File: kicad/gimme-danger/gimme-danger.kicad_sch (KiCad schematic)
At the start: 4 parts, among them U1 ESP32-S3-WROOM-1, U2 TPD6S300RUKR, U3 U261-241N-4BS2SS

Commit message: Set up page details
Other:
- company: (none) -> rbaron.net
- title: (none) -> gimme-danger
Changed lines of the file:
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@@
 (kicad_sch (version 20230121) (generator eeschema)
   (paper "A4")
+  (title_block
+    (title "gimme-danger")
+    (date "2024-01-15")
+    (rev "0.0.1a")
+    (company "rbaron.net")
+  )
   (text "TODO\n- USB resistors (for termination + protection? 100 Ohm?)"
     (at 200.025 144.145 0)

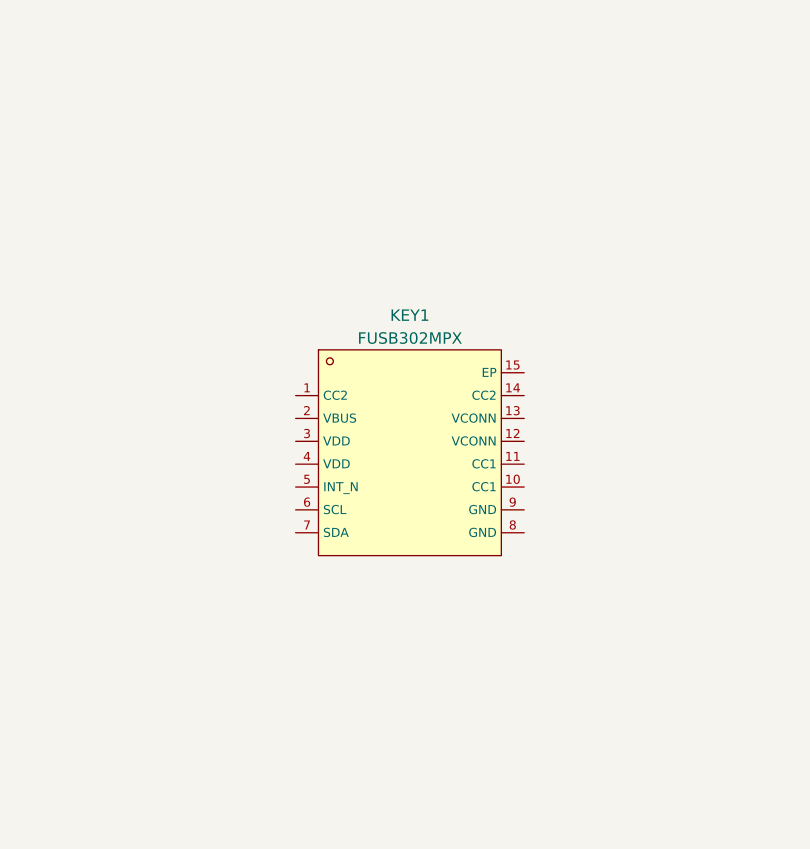
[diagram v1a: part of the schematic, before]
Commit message: Add NX20P5090 IC for switching
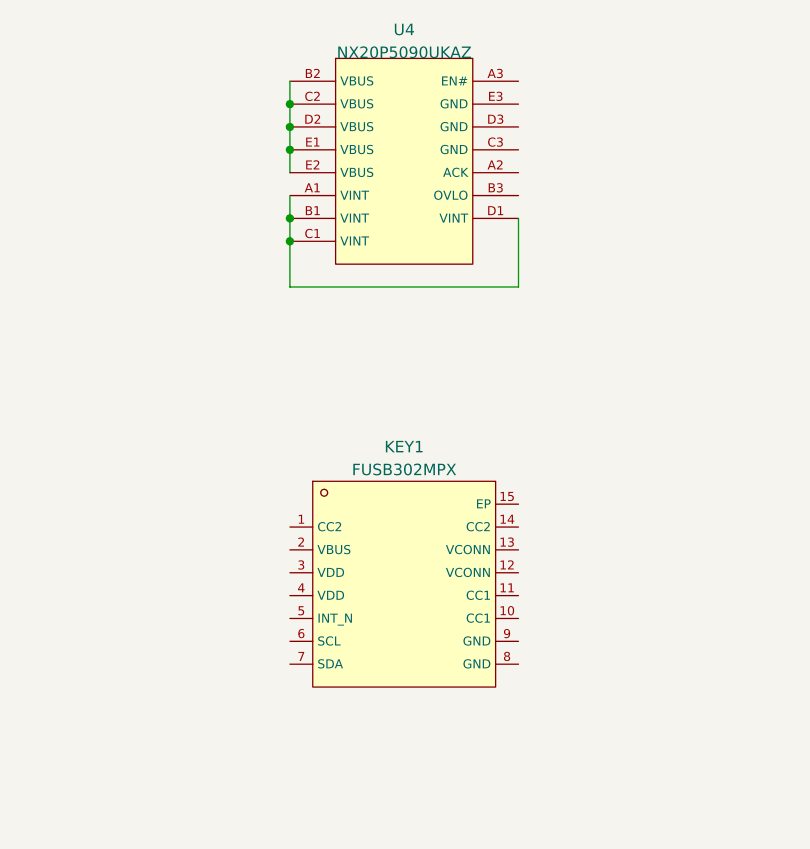
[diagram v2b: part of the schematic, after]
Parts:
- added U4: NX20P5090UKAZ, footprint:WLCSP-15_L2.6-W1.6-R3-C5-P0.50-TL_NXP, symbol NX20P5090UKAZ:NX20P5090UKAZ
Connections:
- new net: U4.A1 (VINT), U4.B1 (VINT), U4.C1 (VINT), U4.D1 (VINT)
- new net: U4.B2 (VBUS), U4.C2 (VBUS), U4.D2 (VBUS), U4.E1 (VBUS), U4.E2 (VBUS)
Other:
- moved on the sheet: KEY1
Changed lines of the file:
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@@
     (company "rbaron.net")
+  )
+  (junction (at 205.105 45.085) (diameter 0) (color 0 0 0 0)
+  )
+  (junction (at 205.105 29.845) (diameter 0) (color 0 0 0 0)
+  )
+  (junction (at 205.105 32.385) (diameter 0) (color 0 0 0 0)
+  )
+  (junction (at 205.105 42.545) (diameter 0) (color 0 0 0 0)
+  )
+  (junction (at 205.105 34.925) (diameter 0) (color 0 0 0 0)
+  )
+  (wire (pts (xy 205.105 40.005) (xy 205.105 42.545))
+    (stroke (width 0) (type default))
+  )
+  (wire (pts (xy 205.105 34.925) (xy 205.105 37.465))
+    (stroke (width 0) (type default))
+  )
+  (wire (pts (xy 205.105 32.385) (xy 205.105 34.925))
+    (stroke (width 0) (type default))
+  )
+  (wire (pts (xy 205.105 45.085) (xy 205.105 50.165))
+    (stroke (width 0) (type default))
+  )
+  (wire (pts (xy 205.105 42.545) (xy 205.105 45.085))
+    (stroke (width 0) (type default))
+  )
+  (wire (pts (xy 205.105 29.845) (xy 205.105 32.385))
+    (stroke (width 0) (type default))
+  )
+  (wire (pts (xy 230.505 50.165) (xy 230.505 42.545))
+    (stroke (width 0) (type default))
+  )
+  (wire (pts (xy 205.105 50.165) (xy 230.505 50.165))
+    (stroke (width 0) (type default))
+  )
+  (wire (pts (xy 205.105 27.305) (xy 205.105 29.845))
+    (stroke (width 0) (type default))
   )
   (text "TODO\n- USB resistors (for termination + protection? 100 Ohm?)"
@@
     )
   )
-  (symbol (lib_id "FUSB302MPX:FUSB302MPX") (at 218.44 68.58 0) (unit 1)
+  (symbol (lib_id "FUSB302MPX:FUSB302MPX") (at 217.805 83.185 0) (unit 1)
     (in_bom yes) (on_board yes) (dnp no) (fields_autoplaced)
-    (property "Reference" "KEY1" (at 218.44 53.34 0)
-      (effects (font (size 1.27 1.27)))
-    )
-    (property "Value" "FUSB302MPX" (at 218.44 55.88 0)
-      (effects (font (size 1.27 1.27)))
-    )
-    (property "Footprint" "footprint:MLP-14_L2.5-W2.5-P0.50-BL-EP" (at 218.44 78.74 0)
+    (property "Reference" "KEY1" (at 217.805 67.945 0)
+      (effects (font (size 1.27 1.27)))
+    )
+    (property "Value" "FUSB302MPX" (at 217.805 70.485 0)
+      (effects (font (size 1.27 1.27)))
+    )
+    (property "Footprint" "footprint:MLP-14_L2.5-W2.5-P0.50-BL-EP" (at 217.805 93.345 0)
       (effects (font (size 1.27 1.27) italic) hide)
     )
-    (property "Datasheet" "https://item.szlcsc.com/444112.html" (at 216.154 68.453 0)
+    (property "Datasheet" "https://item.szlcsc.com/444112.html" (at 215.519 83.058 0)
       (effects (font (size 1.27 1.27)) (justify left) hide)
     )
-    (property "LCSC" "C442699" (at 218.44 68.58 0)
+    (property "LCSC" "C442699" (at 217.805 83.185 0)
       (effects (font (size 1.27 1.27)) hide)
     )
@@
       (effects (font (size 1.27 1.27) italic) hide)
     )
-    (property "Datasheet" "https://item.szlcsc.com/829070.html" (at 107.569 157.353 0)
+    (property "Datasheet" "https://www.ti.com/lit/ds/symlink/tpd6s300.pdf" (at 107.569 157.353 0)
       (effects (font (size 1.27 1.27)) (justify left) hide)
     )
@@
         )
       )
+    )
+  )
+  (symbol (lib_id "NX20P5090UKAZ:NX20P5090UKAZ") (at 217.805 37.465 0) (unit 1)
+    (in_bom yes) (on_board yes) (dnp no) (fields_autoplaced)
+    (property "Reference" "U4" (at 217.805 21.59 0)
+      (effects (font (size 1.27 1.27)))
+    )
+    (property "Value" "NX20P5090UKAZ" (at 217.805 24.13 0)
+      (effects (font (size 1.27 1.27)))
+    )
+    (property "Footprint" "footprint:WLCSP-15_L2.6-W1.6-R3-C5-P0.50-TL_NXP" (at 217.805 47.625 0)
+      (effects (font (size 1.27 1.27) italic) hide)
+    )
+    (property "Datasheet" "https://atta.szlcsc.com/upload/public/pdf/source/20211112/A4F11C05A466D09EAAC4A60A863F24B1.pdf" (at 215.519 37.338 0)
+      (effects (font (size 1.27 1.27)) (justify left) hide)
+    )
+    (property "LCSC" "C2802659" (at 217.805 37.465 0)
+      (effects (font (size 1.27 1.27)) hide)
+    )
+    (pin "E2")
+    (pin "A1")
+    (pin "A2")
+    (pin "A3")
+    (pin "B1")
+    (pin "B2")
+    (pin "B3")
+    (pin "C1")
+    (pin "C2")
+    (pin "C3")
+    (pin "D1")
+    (pin "D2")
+    (pin "D3")
+    (pin "E1")
+    (pin "E3")
+    (instances
+      (project "gimme-danger"
+        (path "/1c42681d-64d0-4eab-a75f-10bf5c65177a"
+          (reference "U4") (unit 1)
+        )
+      )

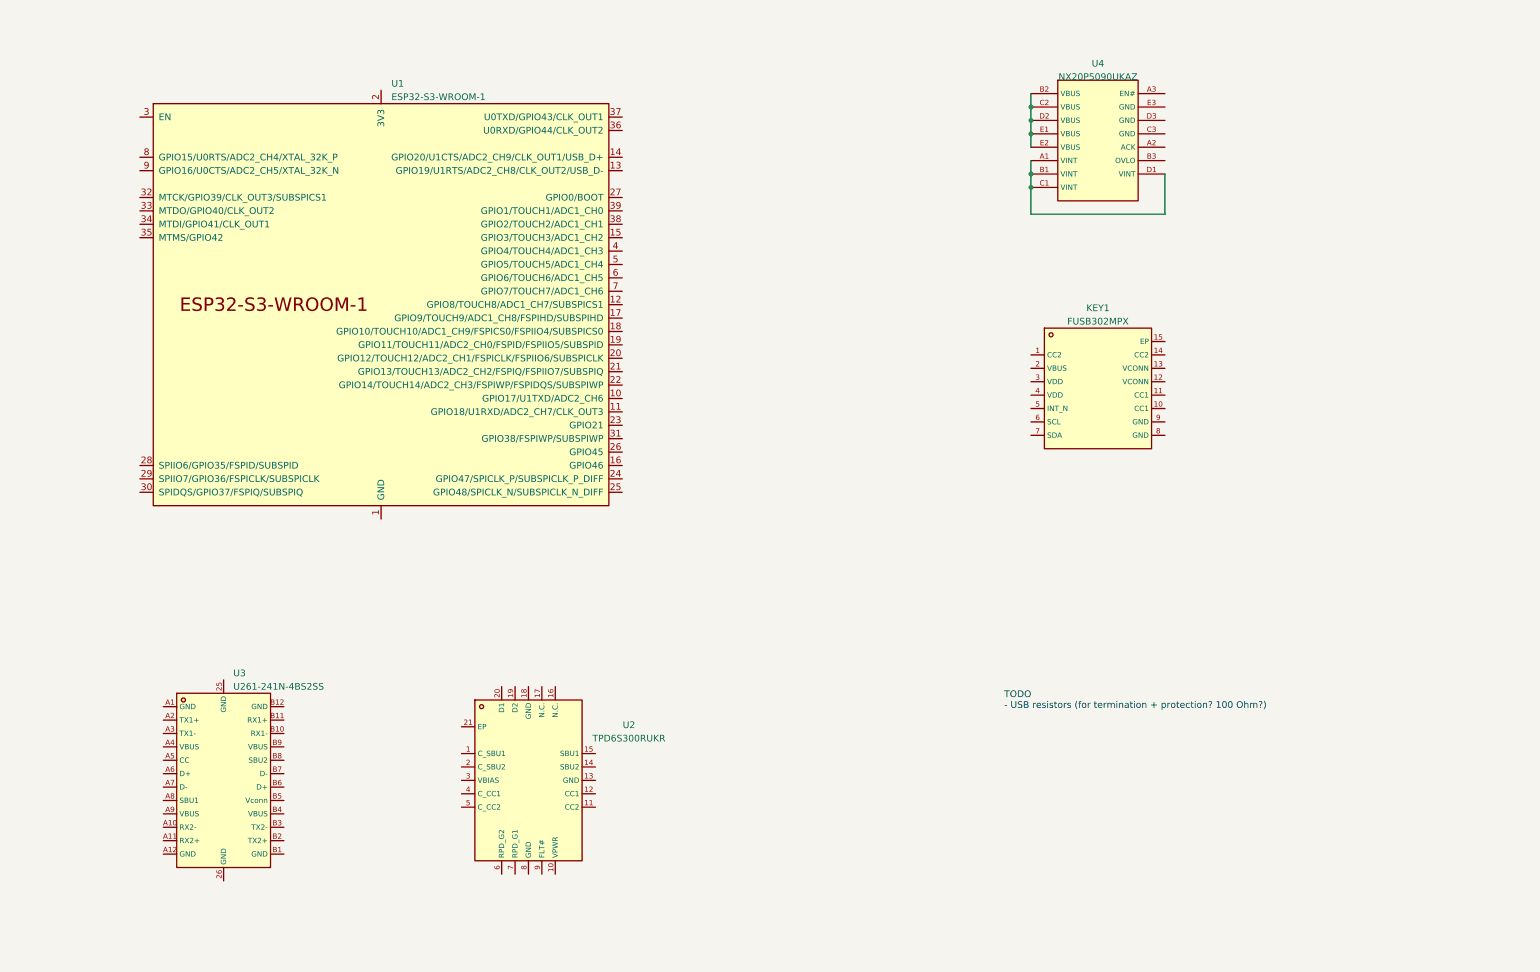
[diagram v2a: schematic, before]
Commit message: First pass on schematics -- needs double checking, esp decoupling caps
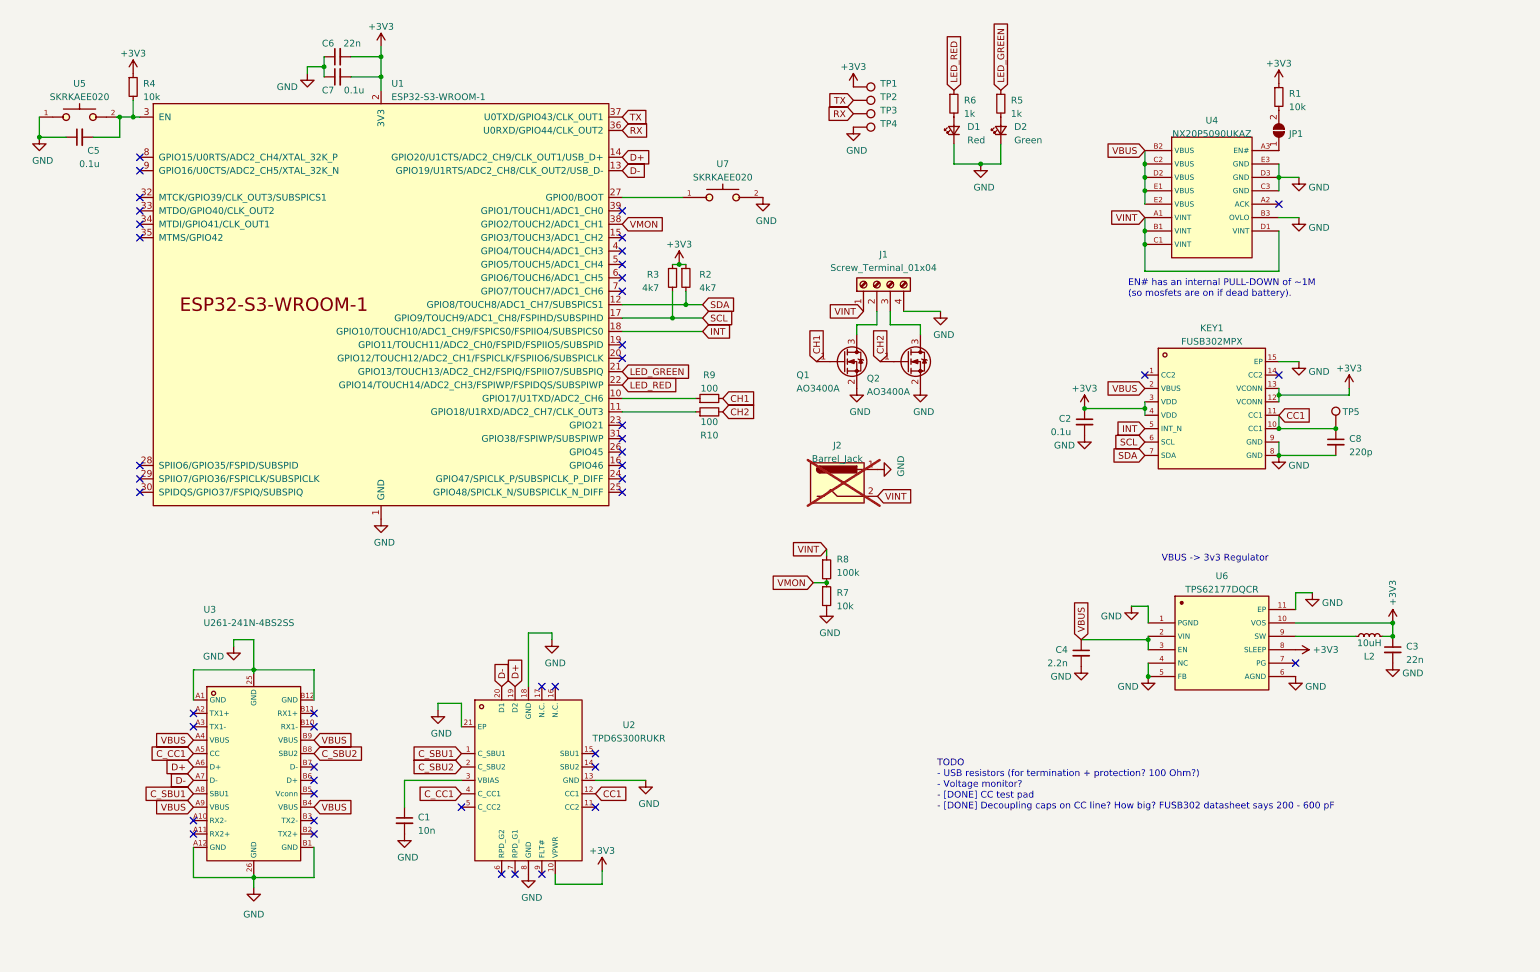
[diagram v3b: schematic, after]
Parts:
- added C1: 10n, Capacitor_SMD:C_0402_1005Metric, symbol Device:C_Small
- added C2, C5, C7: 0.1u, Capacitor_SMD:C_0402_1005Metric, symbol Device:C_Small
- added C3, C6: 22n, Capacitor_SMD:C_0402_1005Metric, symbol Device:C_Small
- added C4: 2.2n, Capacitor_SMD:C_0402_1005Metric, symbol Device:C_Small
- added C8: 220p, Capacitor_SMD:C_0402_1005Metric, symbol Device:C_Small
- added D1: Red, LED_SMD:LED_0603_1608Metric, symbol Device:LED_Small
- added D2: Green, LED_SMD:LED_0603_1608Metric, symbol Device:LED_Small
- added J1: Screw_Terminal_01x04, TerminalBlock_Phoenix:TerminalBlock_Phoenix_MKDS-1,5-4_1x04_P5.00mm_Horizontal, symbol Connector:Screw_Terminal_01x04
- added J2: Barrel_Jack, symbol Connector:Barrel_Jack
- added JP1: ~, Jumper:SolderJumper-2_P1.3mm_Open_RoundedPad1.0x1.5mm, symbol Jumper:SolderJumper_2_Open
- added L2: 10uH, Inductor_SMD:L_0805_2012Metric, symbol Device:L_Small
- added Q1, Q2: AO3400A, Package_TO_SOT_SMD:SOT-23, symbol Transistor_FET:AO3400A
- added R1, R4, R7: 10k, Resistor_SMD:R_0402_1005Metric, symbol Device:R_Small
- added R10, R9: 100, Resistor_SMD:R_0402_1005Metric, symbol Device:R_Small
- added R2, R3: 4k7, Resistor_SMD:R_0402_1005Metric, symbol Device:R_Small
- added R5, R6: 1k, Resistor_SMD:R_0402_1005Metric, symbol Device:R_Small
- added R8: 100k, Resistor_SMD:R_0402_1005Metric, symbol Device:R_Small
- added TP1, TP2, TP3, TP4, TP5: 3v3, TestPoint:TestPoint_Pad_D1.0mm, symbol Connector:TestPoint
- added U5, U7: SKRKAEE020, footprint:SW-SMD_L3.9-W3.0-P4.45, symbol SKRKAEE020:SKRKAEE020
- added U6: TPS62177DQCR, footprint:WSON-10_L3.0-W2.0-P0.50-BL-EP, symbol TPS62177DQCR:TPS62177DQCR
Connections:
- net GND: now reaches U1.1 (GND), U1.40 (GND), U1.41 (GND)
- net GND: now also KEY1.15 (EP), KEY1.8 (GND), KEY1.9 (GND), U2.13 (GND), U2.18 (GND), U2.21 (EP), U2.8 (GND), U3.25 (GND), U3.26 (GND), U3.A1 (GND), U3.A12 (GND), U3.B1 (GND), U3.B12 (GND), U4.B3 (OVLO), U4.C3 (GND), U4.D3 (GND), U4.E3 (GND), C1.2, C2.2, C3.2, C4.2, C5.1, C6.1, C7.1, C8.2, D1.1 (K), D2.1 (K), J1.4 (Pin_4), J2.1, Q1.2 (S), Q2.2 (S), R7.2, TP4.1, U5.1, U6.1 (PGND), U6.11 (EP), U6.4 (NC), U6.5 (FB), U6.6 (AGND), U7.2
- net at U1.10 (GPIO17/U1TXD/ADC2_CH6): now also R9.1
- net at U1.11 (GPIO18/U1RXD/ADC2_CH7/CLK_OUT3): now also R10.1
- net SDA: now reaches U1.12 (GPIO8/TOUCH8/ADC1_CH7/SUBSPICS1)
- net SDA: now also KEY1.7 (SDA), R2.2
- net D-: now reaches U1.13 (GPIO19/U1RTS/ADC2_CH8/CLK_OUT2/USB_D-)
- net D-: now also U2.20 (D1), U3.A7 (D-)
- net D+: now reaches U1.14 (GPIO20/U1CTS/ADC2_CH9/CLK_OUT1/USB_D+)
- net D+: now also U2.19 (D2), U3.A6 (D+)
- net SCL: now reaches U1.17 (GPIO9/TOUCH9/ADC1_CH8/FSPIHD/SUBSPIHD)
- net SCL: now also KEY1.6 (SCL), R3.2
- net INT: now reaches U1.18 (GPIO10/TOUCH10/ADC1_CH9/FSPICS0/FSPIIO4/SUBSPICS0)
- net INT: now also KEY1.5 (INT_N)
- net +3V3: now reaches U1.2 (3V3)
- net +3V3: now also KEY1.12 (VCONN), KEY1.13 (VCONN), KEY1.3 (VDD), KEY1.4 (VDD), U2.10 (VPWR), C2.1, C3.1, C6.2, C7.2, L2.1, R1.1, R2.1, R3.1, R4.1, TP1.1, U6.10 (VOS), U6.8 (SLEEP)
- net LED_GREEN: now reaches U1.21 (GPIO13/TOUCH13/ADC2_CH2/FSPIQ/FSPIIO7/SUBSPIQ)
- net LED_GREEN: now also R5.1
- net LED_RED: now reaches U1.22 (GPIO14/TOUCH14/ADC2_CH3/FSPIWP/FSPIDQS/SUBSPIWP)
- net LED_RED: now also R6.1
- net at U1.27 (GPIO0/BOOT): now also U7.1
- net at U1.3 (EN): now also C5.2, R4.2, U5.2
- net RX: now reaches U1.36 (U0RXD/GPIO44/CLK_OUT2)
- net RX: now also TP3.1
- net TX: now reaches U1.37 (U0TXD/GPIO43/CLK_OUT1)
- net TX: now also TP2.1
- net VMON: now reaches U1.38 (GPIO2/TOUCH2/ADC1_CH1)
- net VMON: now also R7.1, R8.2
- net CC1: now reaches KEY1.10 (CC1)
- net CC1: now also KEY1.11 (CC1), U2.12 (CC1), C8.1, TP5.1
- net VBUS: now reaches KEY1.2 (VBUS)
- net VBUS: now also U3.A4 (VBUS), U3.A9 (VBUS), U3.B4 (VBUS), U3.B9 (VBUS), U4.B2 (VBUS), U4.C2 (VBUS), U4.D2 (VBUS), U4.E1 (VBUS), U4.E2 (VBUS), C4.1, U6.2 (VIN), U6.3 (EN)
- net C_SBU1: now reaches U2.1 (C_SBU1)
- net C_SBU1: now also U3.A8 (SBU1)
- net C_SBU2: now reaches U2.2 (C_SBU2)
- net C_SBU2: now also U3.B8 (SBU2)
- net at U2.3 (VBIAS): now also C1.1
- net C_CC1: now reaches U2.4 (C_CC1)
- net C_CC1: now also U3.A5 (CC)
- net VINT: now reaches U4.A1 (VINT), U4.B1 (VINT), U4.C1 (VINT), U4.D1 (VINT)
- net VINT: now also J1.1 (Pin_1), J2.2, R8.1
- net at U4.A3 (EN#): now also JP1.1 (A)
- new net: L2.2, U6.9 (SW)
- new net: D2.2 (A), R5.2
- new net: J1.3 (Pin_3), Q2.3 (D)
- new net: J1.2 (Pin_2), Q1.3 (D)
- new net: D1.2 (A), R6.2
- new net: JP1.2 (B), R1.2
- new net CH1: Q1.1 (G), R9.2
- new net CH2: Q2.1 (G), R10.2
- no-connect marks 0 -> 47
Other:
- note added: "EN# has an internal PULL-DOWN of ~1M (so mosfets are on if dead battery)."
- note added: "TODO - USB resistors (for termination + protection? 100 Ohm?) - Voltage monitor? - [DONE] CC test pad - [DONE] Decoupling caps on CC line? How big? FUSB302 datasheet says 200 - 600 pF"
- note added: "VBUS -> 3v3 Regulator"
- note removed: "TODO - USB resistors (for termination + protection? 100 Ohm?)"
- moved on the sheet: KEY1, U3, U4

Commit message: Second pass on schematics
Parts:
- added C10, C11, C12, C9: 1u, Capacitor_SMD:C_0402_1005Metric, symbol Device:C_Small
- added C13: 0.1u, Capacitor_SMD:C_0402_1005Metric, symbol Device:C_Small
- added R11: 4k7, Resistor_SMD:R_0402_1005Metric, symbol Device:R_Small
- C1: value 10n -> 100n; LCSC C15195 -> C1525
- C2: LCSC C1525 -> C307331
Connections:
- net +3V3: now also C12.1, C13.2, C9.1, R11.1
- net GND: now also U2.16 (N.C.), U2.17 (N.C.), U2.6 (RPD_G2), U2.7 (RPD_G1), C10.2, C11.2, C12.2, C13.1, C9.2
- net INT: now also R11.2
- net VBUS: now also C11.1
- net VINT: now also C10.1
- net LOAD_EN#: now reaches U1.20 (GPIO12/TOUCH12/ADC2_CH1/FSPICLK/FSPIIO6/SUBSPICLK)
- net LOAD_EN#: now also JP1.2 (B), U4.A3 (EN#)
- net at JP1.1 (A): now also R1.2; no longer U4.A3 (EN#)
- no-connect marks 47 -> 42
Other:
- note added: "EN# has an internal PULL-DOWN of ~1M (so mosfets are on if dead battery). The jumper will let us test off-by-default."
- note added: "ESD, Short-to-VBUS Protection"
- note added: "LEDs"
- note added: "Load switch, reverse current protection"
- note added: "TODO - USB resistors (for termination + protection? 100 Ohm?) - [DONE] Voltage monitor? - [DONE] CC test pad - [DONE] Decoupling caps on CC line? How big? FUSB302 datasheet says 200 - 600 pF - Make sure caps on VBUS/VINT support > 20V (what about surges?)"
- note added: "UART"
- note added: "USB-C Connector"
- note added: "USB-PD PHY"
- note removed: "EN# has an internal PULL-DOWN of ~1M (so mosfets are on if dead battery)."
- note removed: "TODO - USB resistors (for termination + protection? 100 Ohm?) - Voltage monitor? - [DONE] CC test pad - [DONE] Decoupling caps on CC line? How big? FUSB302 datasheet says 200 - 600 pF"
- moved on the sheet: C1, C2, C8, J1, J2, JP1, KEY1, Q1, Q2, R1, R2, R3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
